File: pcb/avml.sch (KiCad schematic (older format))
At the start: 77 parts, among them J1 Video_Output, J10 Front_Conn_1, J11 Front_Conn_3, J12 Back_Conn_2, J13 Back_Conn_3, J14 Back_Conn_1, J15 Front_Conn_4, J16 Back_Conn_4, J17 VIN, J2 Jack_X_CV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

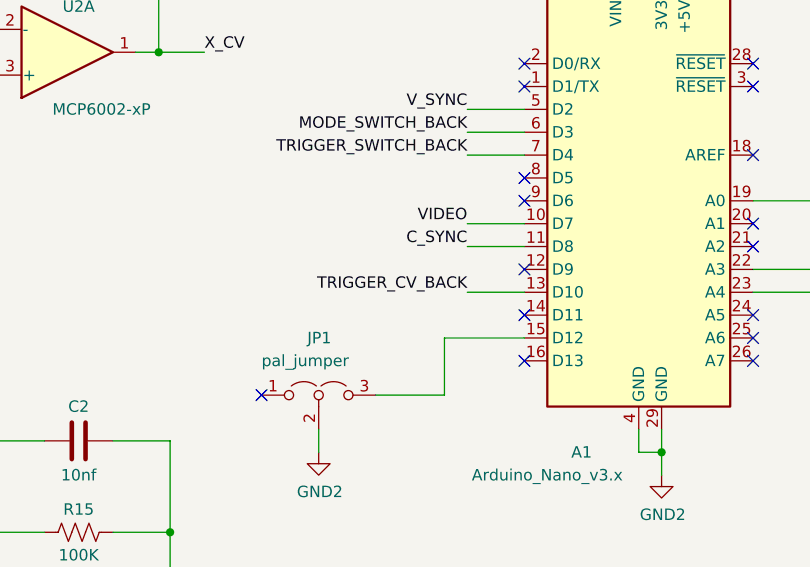
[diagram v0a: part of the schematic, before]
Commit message: Add note about unused sync out and audio out to schematic
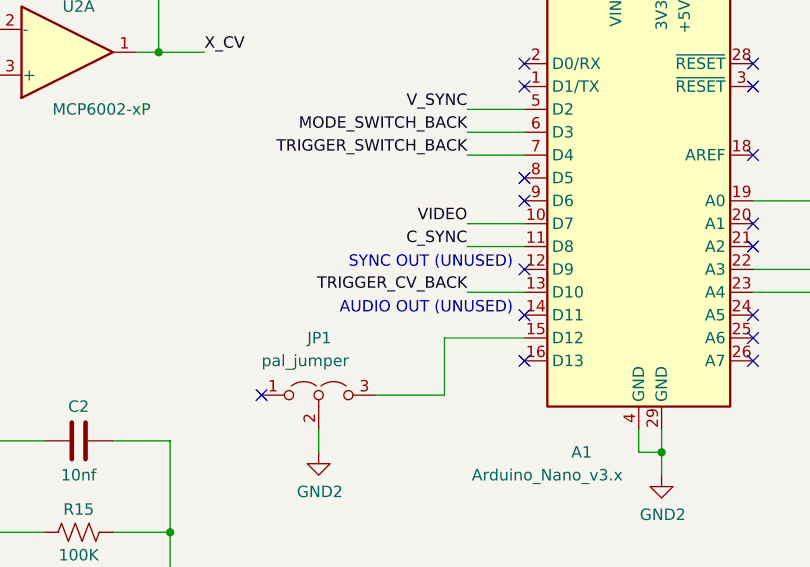
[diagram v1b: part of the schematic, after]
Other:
- note added: "AUDIO OUT (UNUSED)"
- note added: "SYNC OUT (UNUSED)"
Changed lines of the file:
@@
 	6150 8950 6150 9050
 Connection ~ 6150 9050
+Text Notes 10900 2650 2    50   ~ 0
+SYNC OUT (UNUSED)
+Text Notes 10900 2850 2    50   ~ 0
+AUDIO OUT (UNUSED)
 $EndSCHEMATC
